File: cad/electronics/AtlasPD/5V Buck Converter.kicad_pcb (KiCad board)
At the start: 4 copper layers, 37.4 x 20 mm, 16 parts, among them J1 Conn_01x02_Male, J2 Conn_01x02_Male, U1 LM2678T-ADJ_NOPB

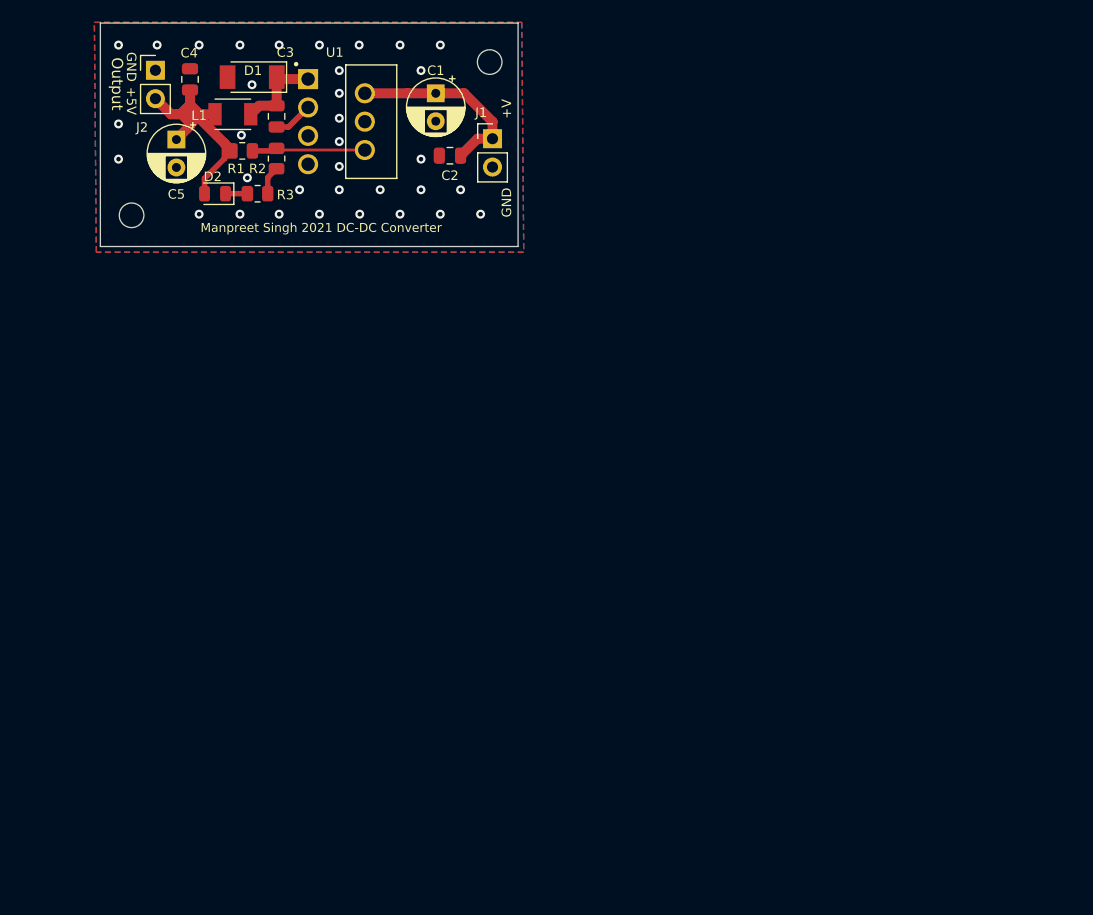
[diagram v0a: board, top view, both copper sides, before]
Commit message: Power board layout
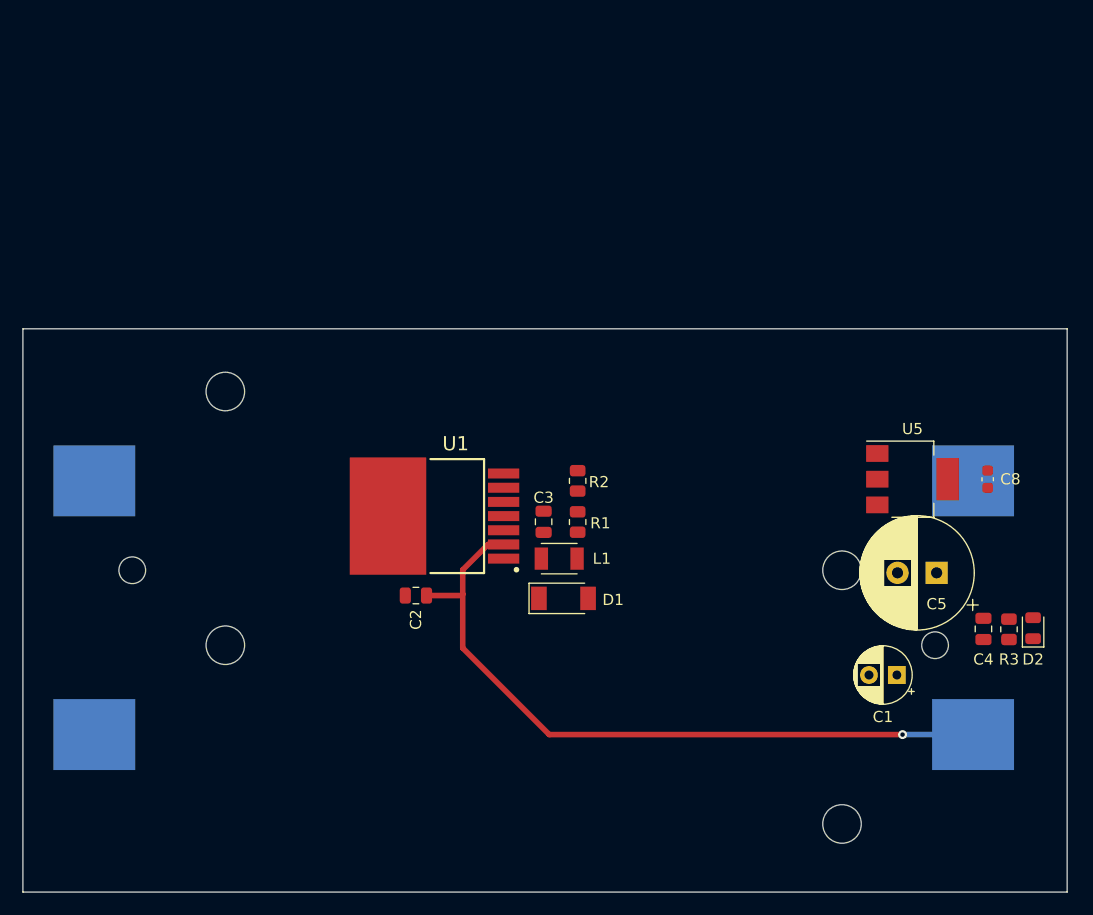
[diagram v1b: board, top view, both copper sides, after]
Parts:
- removed J1, J2: Conn_01x02_Male, Connector_PinHeader_2.54mm:PinHeader_1x02_P2.54mm_Vertical
- removed REF** (x2): MountingHole_2.2mm_M2_DIN965, MountingHole:MountingHole_2.2mm_M2_DIN965
- added BT1: Battery_Cell, Battery:BatteryHolder_Keystone_1042_1x18650, B.Cu at (60.8, 80.8)
- added BT2: Battery_Cell, Battery:BatteryHolder_Keystone_1042_1x18650, B.Cu at (60.8, 58.1)
- added C8: 10uF, Capacitor_SMD:C_0603_1608Metric, F.Cu at (101.5, 57.9)
- added U5: AMS1117-3.3, Package_TO_SOT_SMD:SOT-223-3_TabPin2, F.Cu at (94.7, 57.9)
- C5: footprint Capacitor_THT:CP_Radial_D5.0mm_P2.50mm -> Capacitor_THT:CP_Radial_D10.0mm_P3.50mm
- U1: footprint LM2678:TO127P1041X469X2199-7N -> SamacSys_Parts:TO127P1435X464-8N
- moved C4 86.4 mm to (101.1, 71.3), turned to 270 degrees
- moved D2 82.9 mm to (105.5, 71.2), turned to 90 degrees
- moved C5 78.3 mm to (96.9, 66.3), turned to 180 degrees
- moved R3 77.7 mm to (103.4, 71.4), turned to 90 degrees
- moved C1 66.4 mm to (93.3, 75.4), turned to 180 degrees
- moved D1 54.3 mm to (63.5, 68.6), turned to 0 degrees
- moved L1 49.3 mm to (63.1, 65.0), turned to 0 degrees
- moved R1 44.8 mm to (64.8, 61.7), turned to 90 degrees
- moved C3 43.5 mm to (61.7, 61.7), turned to 90 degrees
- moved C2 39.5 mm to (50.3, 68.3)
- moved R2 39.5 mm to (64.8, 58.1), turned to 90 degrees
- moved U1 35.9 mm to (51.9, 61.2), turned to 180 degrees
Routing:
- net +BATT: track 0.00 -> 63.8 mm, vias 0 -> 1
- net /Sheet60A23886/Output: track 28.4 -> 0.00 mm
- net Net-(C1-Pad1): track 17.5 -> 0.00 mm
- net Net-(R1-Pad2): track 10.2 -> 0.00 mm
- net Net-(C3-Pad1): track 8.08 -> 0.00 mm
- net Net-(C3-Pad2): track 3.54 -> 0.00 mm
- net GND: track 2.56 -> 0.00 mm, vias 34 -> 0
- net Net-(D2-Pad1): track 1.96 -> 0.00 mm
- removed copper zone on B.Cu, net GND
- removed copper zone on F.Cu, net GND
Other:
- board size 37.4 x 20 mm -> 93.5 x 50.4 mm
- board text removed: "+5V"
- board text removed: "+V"
- board text removed: "GND"
- board text removed: "JLCJLCJLCJLC"
- board text removed: "Manpreet Singh 2021 DC-DC Converter"
- board text removed: "Output"

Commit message: First Board Layout done
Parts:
- added J1: Conn_01x02_Male, Connector_JST:JST_PH_B2B-PH-K_1x02_P2.00mm_Vertical, F.Cu at (104.7, 50.8)
- added J2: Conn_01x02_Male, Connector_JST:JST_PH_B2B-PH-K_1x02_P2.00mm_Vertical, F.Cu at (104.7, 66.6)
- moved C2 28.2 mm to (78.5, 68.9), turned to 270 degrees
- moved C3 20.3 mm to (82.1, 62.1)
- moved D1 20.3 mm to (83.8, 68.9)
- moved L1 20.3 mm to (83.5, 65.4)
- moved U1 20.3 mm to (72.3, 61.5)
- moved R1 19.5 mm to (84.3, 62.1)
- moved R2 19.5 mm to (84.3, 58.4)
- moved C8 4.58 mm to (105.0, 55.0)
- moved U5 4.57 mm to (90.2, 57.9)
- moved C1 4.16 mm to (92.2, 79.4), turned to 270 degrees
- moved C5 0.61 mm to (97.5, 66.0)
- moved D2 0.10 mm to (105.5, 71.3)
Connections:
- U1 pad 8: (no net) -> GND
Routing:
- net +5V: track 0.00 -> 37.6 mm
- net +3V3: track 0.00 -> 27.0 mm
- net +BATT: track 63.8 -> 74.6 mm, vias 1 -> 0
- net Net-(C3-Pad1): track 0.00 -> 9.46 mm
- net Net-(R1-Pad2): track 0.00 -> 7.75 mm
- net GND: track 0.00 -> 4.81 mm, vias 0 -> 133
- net Net-(C3-Pad2): track 0.00 -> 4.29 mm
- net Net-(D2-Pad1): track 0.00 -> 2.17 mm
- added copper zone on B.Cu, net GND
- added copper zone on F.Cu, net GND
- added copper zone on B.Cu, net Net-(BT1-Pad2)
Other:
- copper layers 4 -> 2

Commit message: Layout updates
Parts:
- removed J1, J2: Conn_01x02_Male, Connector_JST:JST_PH_B2B-PH-K_1x02_P2.00mm_Vertical
- added J5: Conn_01x04, Connector_JST:JST_PH_B4B-PH-K_1x04_P2.00mm_Vertical, F.Cu at (104.9, 66.6)
- moved C10 12.4 mm to (106.6, 60.2), turned to 90 degrees
- moved D6 11.7 mm to (102.2, 60.2), turned to 270 degrees
- moved R12 11.2 mm to (104.3, 60.2), turned to 270 degrees
- moved C8 9.16 mm to (96.0, 56.6), turned to 90 degrees
- renumbered C4 to C10, C5 to C11, C1 to C6, C2 to C7, C3 to C9, D1 to D5, D2 to D6, R1 to R10, R2 to R11, R3 to R12, U5 to U6, U1 to U7
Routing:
- net +BATT: track 74.6 -> 96.8 mm, vias 0 -> 9
- net +3V3: track 27.0 -> 9.15 mm
- net +5V: track 37.6 -> 40.4 mm
- net GND: track 4.81 -> 3.50 mm, vias 133 -> 132
- added copper zone on F.Cu, net +BATT

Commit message: Battery board changes
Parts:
- renumbered BT1 to BT401, BT2 to BT402, C6 to C401, C7 to C402, C8 to C403, C9 to C404, C10 to C405, C11 to C406, D5 to D401, D6 to D402, J5 to J401, L1 to L401, R10 to R401, R11 to R402, R12 to R403, U6 to U401, U7 to U402
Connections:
- net Net-(C9-Pad1) renamed /SWITCH_OUT
- net Net-(C9-Pad2) renamed /CB
- net Net-(R10-Pad2) renamed /FEEDBACK
- U402 pad 8: GND -> (no net)
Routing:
- net GND: vias 132 -> 131

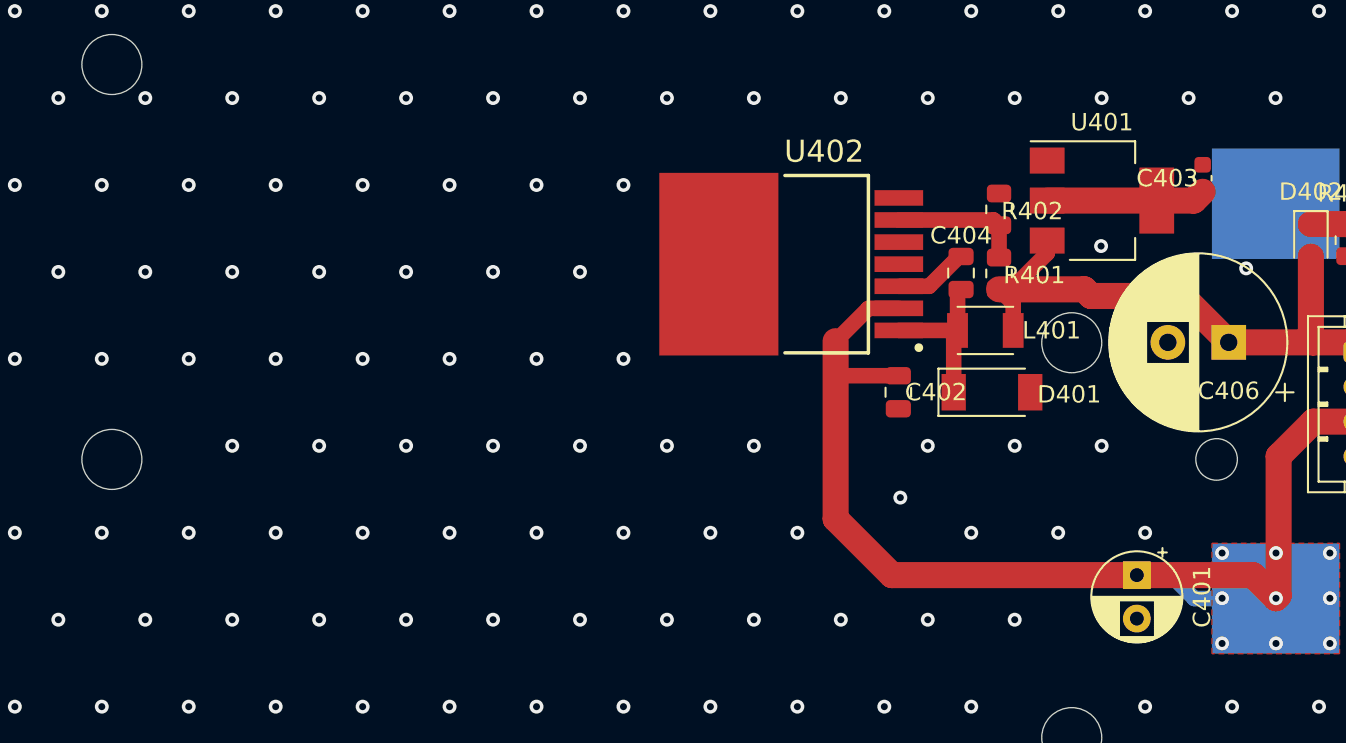
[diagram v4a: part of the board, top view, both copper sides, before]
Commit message: More changes to battery board, preping for manufacturing
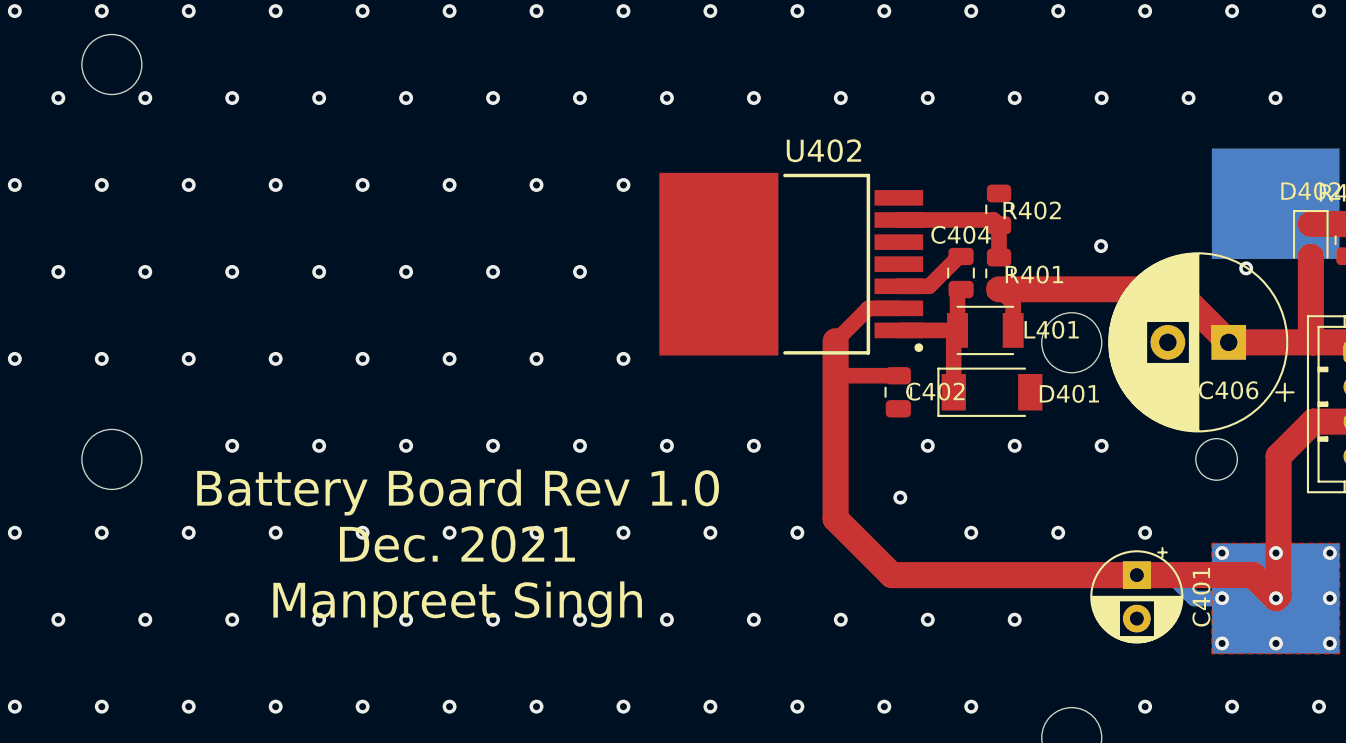
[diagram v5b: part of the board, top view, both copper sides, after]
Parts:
- removed C403: 10uF, Capacitor_SMD:C_0603_1608Metric
- removed U401: AMS1117-3.3, Package_TO_SOT_SMD:SOT-223-3_TabPin2
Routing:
- net +3V3: track 9.15 -> 0.00 mm
- net +5V: track 40.4 -> 36.7 mm
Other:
- board text added: "Battery Board Rev 1.0 Dec. 2021 Manpreet Singh"

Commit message: Battery board sent to fab
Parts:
- L401: footprint Inductor_SMD:L_TDK_NLV32_3.2x2.5mm -> SamacSys_Parts:CDRH127
- U402: value LM2678T-ADJ_NOPB -> LM2678S-ADJ_NOPB
- moved R402 16.4 mm to (68.3, 62.2), turned to 180 degrees
- moved R401 15.6 mm to (69.1, 58.5), turned to 270 degrees
- moved U402 10.3 mm to (71.9, 71.9), turned to 270 degrees
- moved L401 10.0 mm to (84.1, 55.4), turned to 90 degrees
- moved R403 7.72 mm to (104.5, 52.5), turned to 180 degrees
- moved C404 7.53 mm to (74.5, 62.4), turned to 180 degrees
- moved D402 5.77 mm to (104.5, 54.9), turned to 180 degrees
- moved C402 5.58 mm to (78.7, 74.5)
- moved D401 4.17 mm to (81.4, 65.5)
- moved C405 2.81 mm to (104.4, 62.0), turned to 0 degrees
- moved C406 2.01 mm to (96.0, 67.4), turned to 90 degrees
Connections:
- U402 pad 8: (no net) -> GND
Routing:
- net +BATT: track 96.8 -> 59.7 mm, vias 9 -> 5
- net +5V: track 36.7 -> 63.7 mm
- net /SWITCH_OUT: track 9.46 -> 15.5 mm
- net GND: track 3.50 -> 0.00 mm, vias 131 -> 129
- net /FEEDBACK: track 7.75 -> 6.33 mm
- net /CB: track 4.29 -> 3.45 mm

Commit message: Battery board Rev 1.5
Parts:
- removed C406: 1000uF, Capacitor_THT:CP_Radial_D10.0mm_P3.50mm
- removed R402, R403: 1k, Resistor_SMD:R_0805_2012Metric
- C405: value 10uF -> 220uF; footprint Capacitor_SMD:C_0805_2012Metric -> Capacitor_THT:CP_Radial_D5.0mm_P2.50mm
- L401: value 22 uH -> 39 uH
- R401: value 3.16k -> 1k
- U402: value LM2678S-ADJ_NOPB -> AP1509-50SG-13; footprint SamacSys_Parts:TO127P1435X464-8N -> Package_SO:SO-8_3.9x4.9mm_P1.27mm
- moved R401 28.8 mm to (97.6, 62.4), turned to 180 degrees
- moved C404 23.7 mm to (97.6, 67.9)
- moved C401 13.8 mm to (103.8, 86.8)
- moved D402 12.4 mm to (97.6, 65.1), turned to 0 degrees
- moved D401 10.2 mm to (72.3, 61.0), turned to 180 degrees
- moved C402 10.0 mm to (82.7, 65.3), turned to 0 degrees
- moved C405 9.77 mm to (103.8, 52.2), turned to 90 degrees
- moved U402 6.23 mm to (76.7, 67.9)
- moved L401 0.40 mm to (84.2, 55.0)
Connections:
- C404 pad 1: /SWITCH_OUT -> +5V
- C404 pad 2: /CB -> GND
- D401 pad 1: /SWITCH_OUT -> Net-(D401-Pad1)
- L401 pad 1: /SWITCH_OUT -> Net-(D401-Pad1)
- R401 pad 1: +5V -> Net-(D402-Pad1)
- R401 pad 2: /FEEDBACK -> GND
- U402 pad 1: /SWITCH_OUT -> +BATT
- U402 pad 2: +BATT -> Net-(D401-Pad1)
- U402 pad 3: /CB -> +5V
- U402 pad 5: (no net) -> GND
- U402 pad 6: /FEEDBACK -> GND
- U402 pad 7: Net-(U402-Pad7) -> GND
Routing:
- net /SWITCH_OUT: track 15.5 -> 0.00 mm
- net Net-(D401-Pad1): track 0.00 -> 14.0 mm
- net +5V: track 63.7 -> 72.8 mm, vias 0 -> 1
- net +BATT: track 59.7 -> 51.7 mm
- net /FEEDBACK: track 6.33 -> 0.00 mm
- net /CB: track 3.45 -> 0.00 mm
- net Net-(D402-Pad1): track 2.43 -> 3.50 mm
- net GND: vias 129 -> 144
